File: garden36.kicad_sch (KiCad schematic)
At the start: 42 parts, among them J1 Conn_01x02, SW1 SW_SPDT, SW2 SW_Push, U1 nice_nano

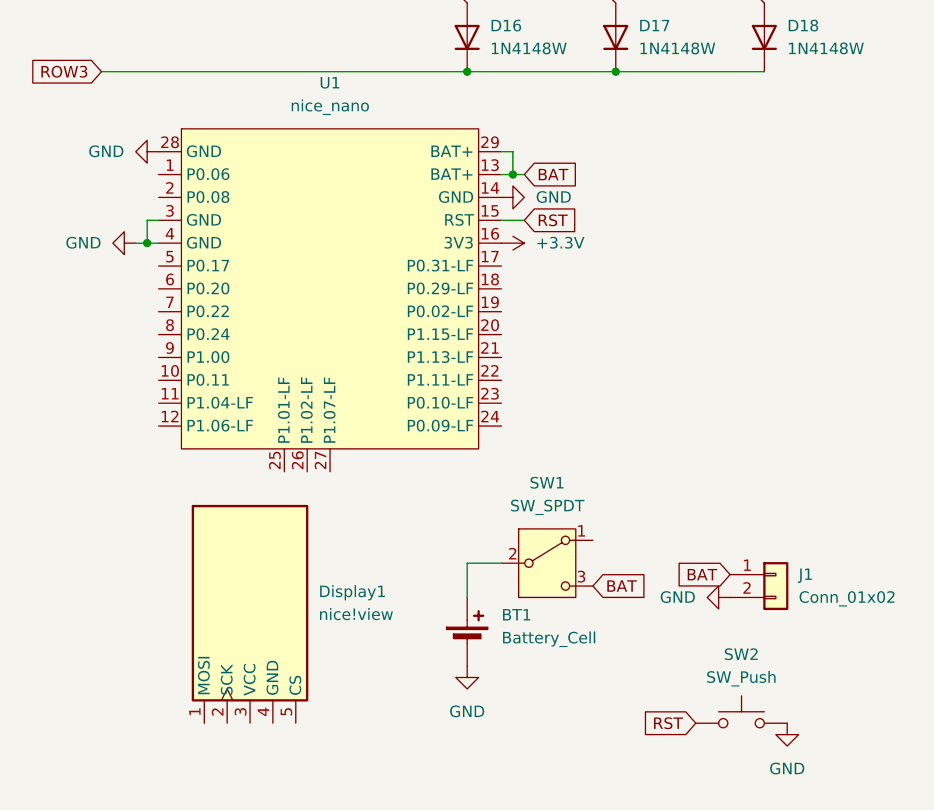
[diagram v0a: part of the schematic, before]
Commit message: Add .gitignore and ready schema
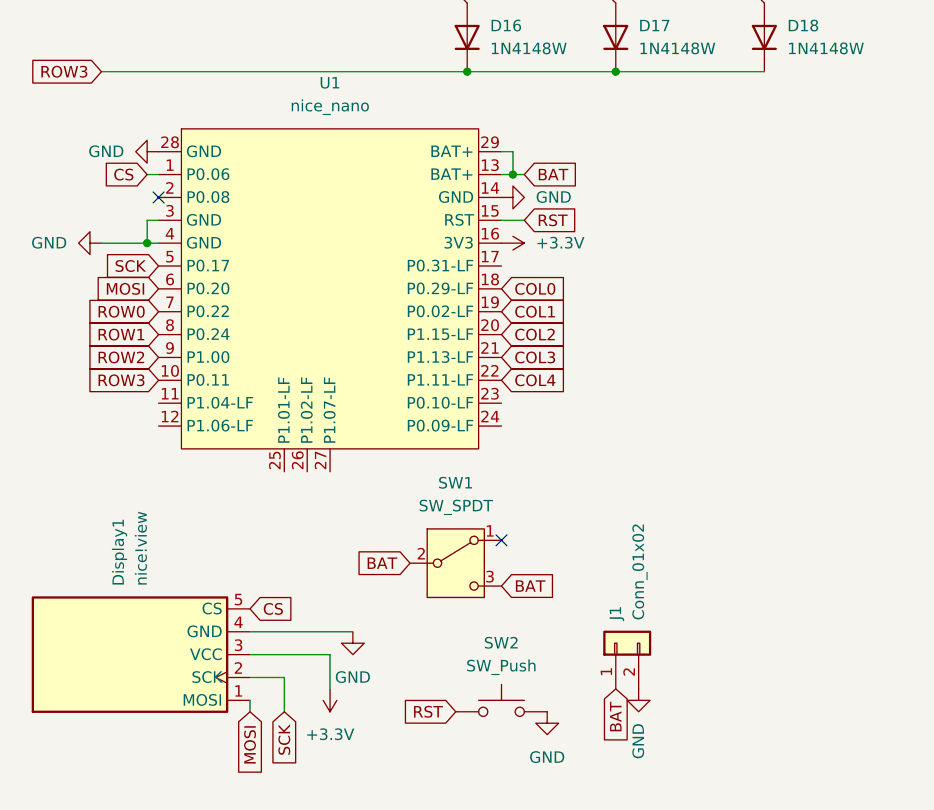
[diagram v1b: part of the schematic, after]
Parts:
- removed BT1: Battery_Cell, symbol Device:Battery_Cell
- J1: footprint (none) -> PCM_marbastlib-various:CON_JST_ACH_BM02B
- SW1: footprint (none) -> Button_Switch_SMD:SW_SPDT_CK_JS102011SAQN
- SW2: footprint (none) -> Button_Switch_SMD:SW_Tactile_SPST_NO_Straight_CK_PTS636Sx25SMTRLFS
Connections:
- net +3.3V: now also Display1.3 (VCC)
- net BAT: now also SW1.2 (B)
- net COL0: now also U1.18 (P0.29-LF)
- net COL1: now also U1.19 (P0.02-LF)
- net COL2: now also U1.20 (P1.15-LF)
- net COL3: now also U1.21 (P1.13-LF)
- net COL4: now also U1.22 (P1.11-LF)
- net GND: now also Display1.4 (GND)
- net ROW0: now also U1.7 (P0.22)
- net ROW1: now also U1.8 (P0.24)
- net ROW2: now also U1.9 (P1.00)
- net ROW3: now also U1.10 (P0.11)
- net CS: now reaches U1.1 (P0.06)
- net CS: now also Display1.5 (CS)
- net SCK: now reaches U1.5 (P0.17)
- net SCK: now also Display1.2 (SCK)
- net MOSI: now reaches U1.6 (P0.20)
- net MOSI: now also Display1.1 (MOSI)
- no-connect marks 1 -> 3
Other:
- moved on the sheet: Display1, J1, SW1, SW2

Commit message: Move PCB board around
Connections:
- no-connect marks 3 -> 10
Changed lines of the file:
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@@
+	)
+	(no_connect
+		(at 67.31 154.94)
+	)
+	(no_connect
+		(at 67.31 152.4)
 	)
 	(no_connect
@@
 	)
 	(no_connect
-		(at 72.39 80.01)
+		(at 45.72 160.02)
+	)
+	(no_connect
+		(at 48.26 160.02)
+	)
+	(no_connect
+		(at 67.31 137.16)
+	)
+	(no_connect
+		(at 29.21 154.94)
+	)
+	(no_connect
+		(at 43.18 160.02)
 	)
 	(no_connect
 		(at 29.21 129.54)
 	)
+	(no_connect
+		(at 29.21 152.4)
+	)
 	(wire

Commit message: Finished basic layout without any routing
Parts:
- SW1: footprint Button_Switch_SMD:SW_SPDT_CK_JS102011SAQN -> PCM_marbastlib-various:SW_MSK12C02-HB
- SW2: footprint Button_Switch_SMD:SW_Tactile_SPST_NO_Straight_CK_PTS636Sx25SMTRLFS -> Button_Switch_SMD:SW_SPST_TL3305A
- U1: footprint PCM_marbastlib-xp-promicroish:nice_nano_AH_USBup -> PCM_marbastlib-xp-promicroish:nice_nano_AH_USBdn
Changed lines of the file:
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@@
 			)
 		)
-		(property "Footprint" "Button_Switch_SMD:SW_SPDT_CK_JS102011SAQN"
+		(property "Footprint" "PCM_marbastlib-various:SW_MSK12C02-HB"
 			(at 63.246 165.608 0)
 			(effects
@@
 			)
 		)
-		(property "Footprint" "Button_Switch_SMD:SW_Tactile_SPST_NO_Straight_CK_PTS636Sx25SMTRLFS"
+		(property "Footprint" "Button_Switch_SMD:SW_SPST_TL3305A"
 			(at 67.31 181.61 0)
 			(effects
@@
 			)
 		)
-		(property "Footprint" "PCM_marbastlib-xp-promicroish:nice_nano_AH_USBup"
+		(property "Footprint" "PCM_marbastlib-xp-promicroish:nice_nano_AH_USBdn"
 			(at 48.26 171.45 0)
 			(effects

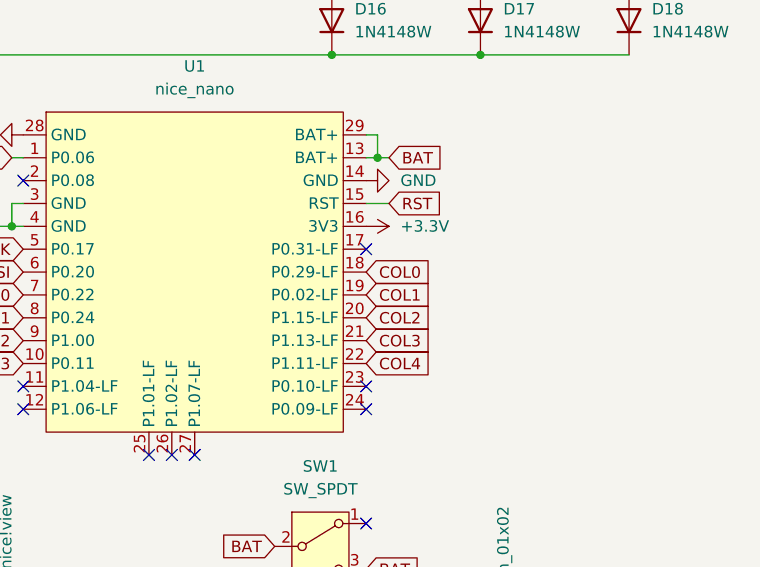
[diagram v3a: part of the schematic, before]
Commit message: Finished trace routing for left part
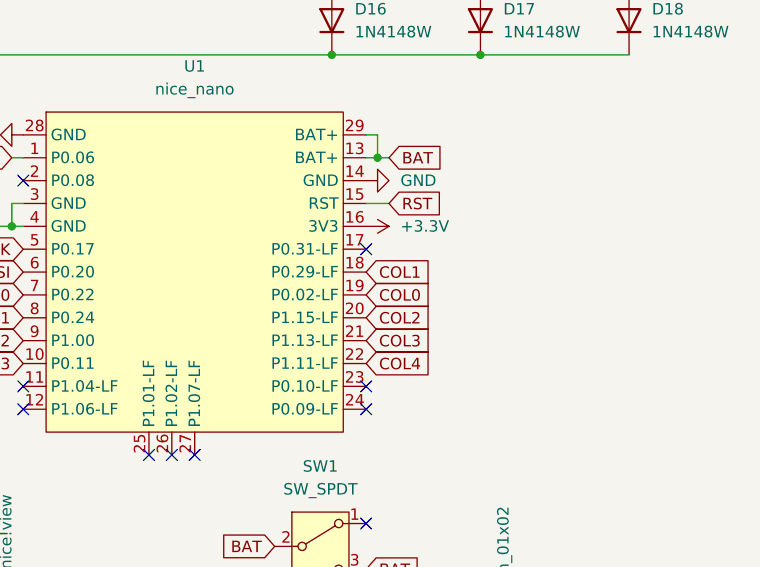
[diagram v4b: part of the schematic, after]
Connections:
- net COL0: now also U1.19 (P0.02-LF); no longer U1.18 (P0.29-LF)
- net COL1: now also U1.18 (P0.29-LF); no longer U1.19 (P0.02-LF)
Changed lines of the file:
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@@
 		)
 	)
-	(global_label "COL1"
+	(global_label "COL0"
 		(shape input)
 		(at 67.31 142.24 0)
@@
 		)
 	)
-	(global_label "COL0"
+	(global_label "COL1"
 		(shape input)
 		(at 67.31 139.7 0)

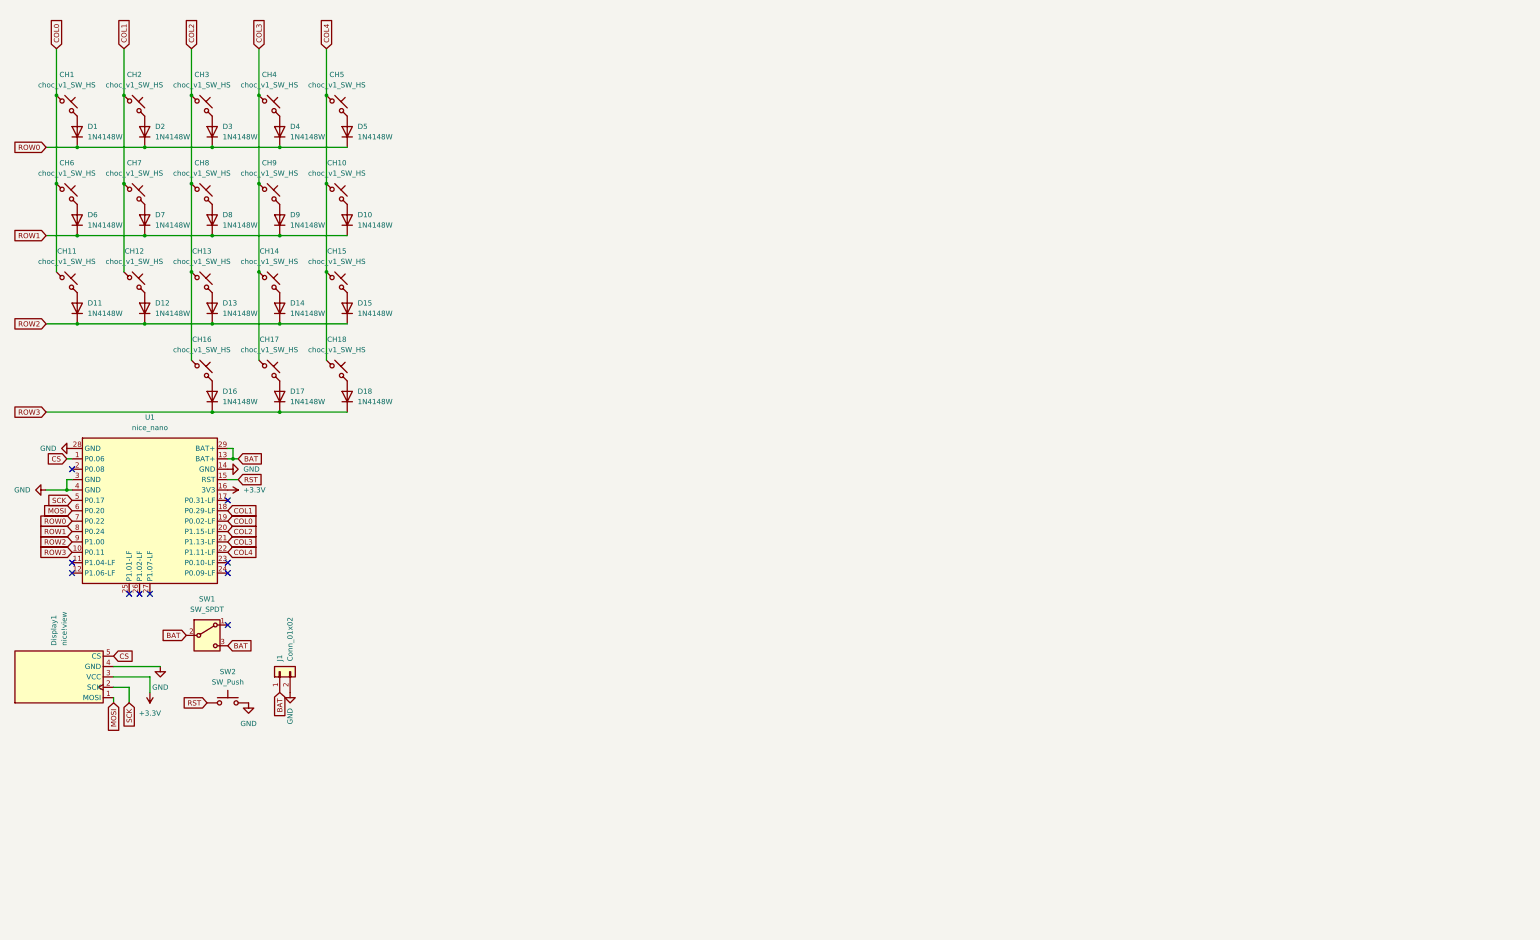
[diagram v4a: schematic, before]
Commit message: Add right half of keyboard
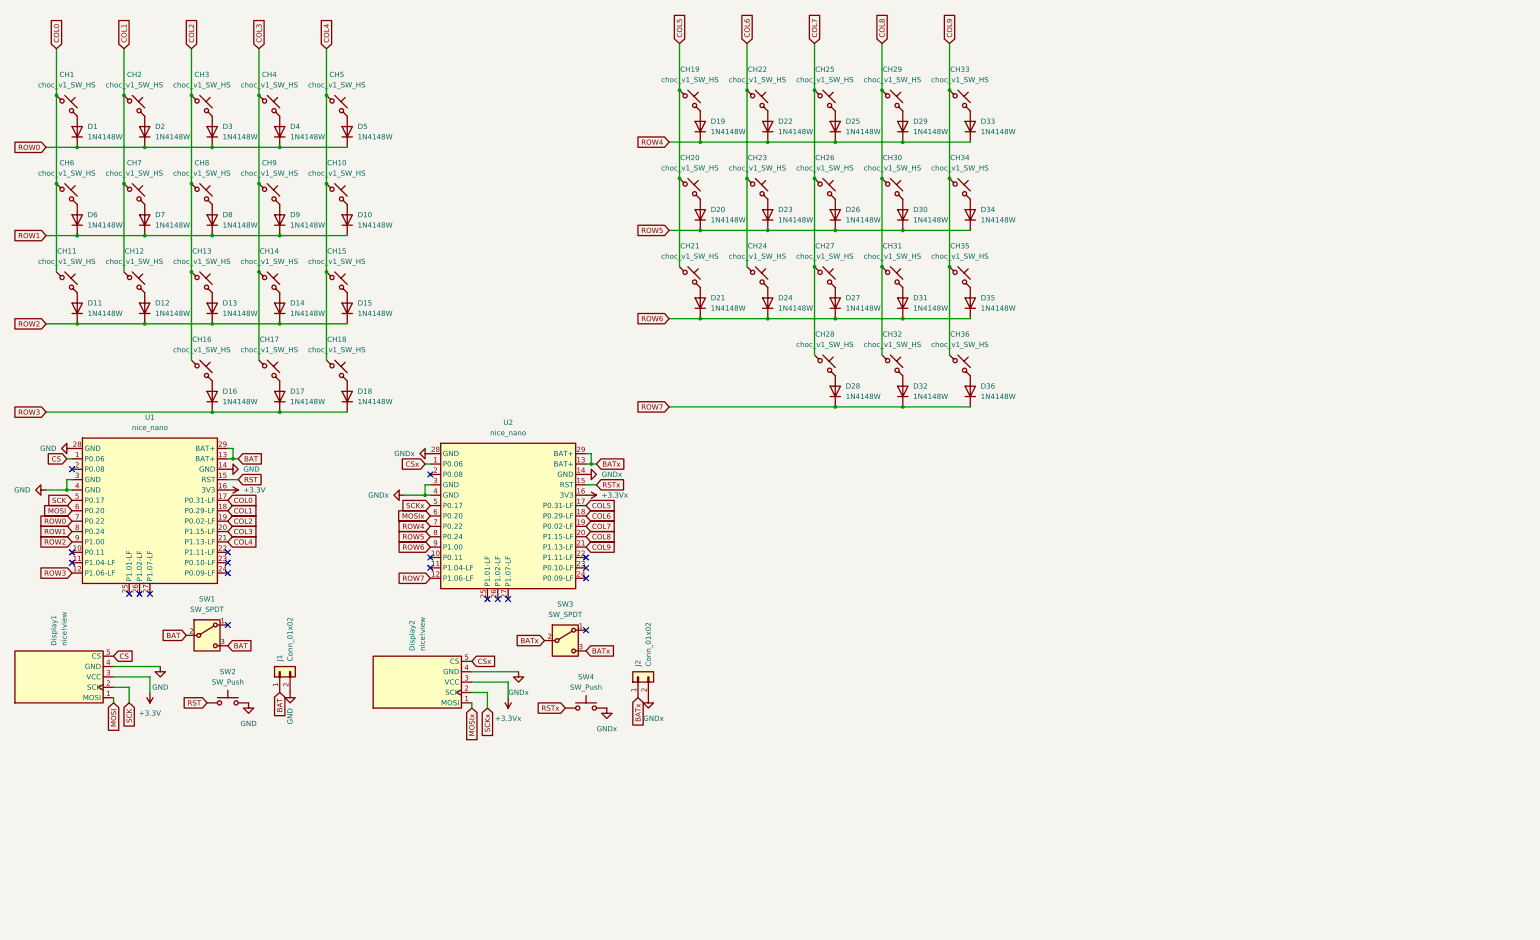
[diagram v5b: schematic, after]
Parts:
- added CH19, CH20, CH21, CH22, CH23, CH24, CH25, CH26, CH27, CH28, CH29, CH30, CH31, CH32, CH33, CH34, CH35, CH36: choc_v1_SW_HS, PCM_marbastlib-choc:SW_choc_v1_HS_CPG135001S30_1u, symbol PCM_marbastlib-choc:choc_v1_SW_HS_CPG135001S30
- added D19, D20, D21, D22, D23, D24, D25, D26, D27, D28, D29, D30, D31, D32, D33, D34, D35, D36: 1N4148W, Diode_SMD:D_SOD-123, symbol Diode:1N4148W
- added Display2: nice!view, nice_view:nice_view, symbol nice_view:nice!view
- added J2: Conn_01x02, PCM_marbastlib-various:CON_JST_ACH_BM02B, symbol Connector_Generic:Conn_01x02
- added SW3: SW_SPDT, PCM_marbastlib-various:SW_MSK12C02-HB, symbol Switch:SW_SPDT
- added SW4: SW_Push, Button_Switch_SMD:SW_SPST_TL3305A, symbol Switch:SW_Push
- added U2: nice_nano, PCM_marbastlib-xp-promicroish:nice_nano_AH_USBdn, symbol PCM_marbastlib-promicroish:nice_nano
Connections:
- net COL0: now also U1.17 (P0.31-LF); no longer U1.19 (P0.02-LF)
- net COL2: now also U1.19 (P0.02-LF); no longer U1.20 (P1.15-LF)
- net COL3: now also U1.20 (P1.15-LF); no longer U1.21 (P1.13-LF)
- net COL4: now also U1.21 (P1.13-LF); no longer U1.22 (P1.11-LF)
- net ROW3: now also U1.12 (P1.06-LF); no longer U1.10 (P0.11)
- new net: CH20.2, D20.2 (A)
- new net: CH24.2, D24.2 (A)
- new net: CH32.2, D32.2 (A)
- new net: CH23.2, D23.2 (A)
- new net: CH29.2, D29.2 (A)
- new net: CH22.2, D22.2 (A)
- new net: CH25.2, D25.2 (A)
- new net: CH31.2, D31.2 (A)
- new net: CH34.2, D34.2 (A)
- new net: CH36.2, D36.2 (A)
- new net: CH21.2, D21.2 (A)
- new net: CH30.2, D30.2 (A)
- new net: CH33.2, D33.2 (A)
- new net: CH35.2, D35.2 (A)
- new net: CH26.2, D26.2 (A)
- new net: CH19.2, D19.2 (A)
- new net: CH28.2, D28.2 (A)
- new net: CH27.2, D27.2 (A)
- new net +3.3Vx: Display2.3 (VCC), U2.16 (3V3)
- new net BATx: J2.1 (Pin_1), SW3.2 (B), SW3.3 (C), U2.13 (BAT+), U2.29 (BAT+)
- new net COL5: CH19.1, CH20.1, CH21.1, U2.17 (P0.31-LF)
- new net COL6: CH22.1, CH23.1, CH24.1, U2.18 (P0.29-LF)
- new net COL7: CH25.1, CH26.1, CH27.1, CH28.1, U2.19 (P0.02-LF)
- new net COL8: CH29.1, CH30.1, CH31.1, CH32.1, U2.20 (P1.15-LF)
- new net COL9: CH33.1, CH34.1, CH35.1, CH36.1, U2.21 (P1.13-LF)
- new net CSx: Display2.5 (CS), U2.1 (P0.06)
- new net GNDx: Display2.4 (GND), J2.2 (Pin_2), SW4.2, U2.14 (GND), U2.28 (GND), U2.3 (GND), U2.4 (GND)
- new net MOSIx: Display2.1 (MOSI), U2.6 (P0.20)
- new net ROW4: D19.1 (K), D22.1 (K), D25.1 (K), D29.1 (K), D33.1 (K), U2.7 (P0.22)
- new net ROW5: D20.1 (K), D23.1 (K), D26.1 (K), D30.1 (K), D34.1 (K), U2.8 (P0.24)
- new net ROW6: D21.1 (K), D24.1 (K), D27.1 (K), D31.1 (K), D35.1 (K), U2.9 (P1.00)
- new net ROW7: D28.1 (K), D32.1 (K), D36.1 (K), U2.12 (P1.06-LF)
- new net RSTx: SW4.1, U2.15 (RST)
- new net SCKx: Display2.2 (SCK), U2.5 (P0.17)
- no-connect marks 10 -> 20
